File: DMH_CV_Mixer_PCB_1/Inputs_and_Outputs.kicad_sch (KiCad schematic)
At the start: 13 parts, among them J1 TS_Jack_6.35mm_Sw, J10 TS_Jack_6.35mm_Sw, J11 TS_Jack_6.35mm_Sw, J12 TS_Jack_6.35mm_Sw, J2 TS_Jack_6.35mm_Sw, J3 TS_Jack_6.35mm_Sw, J4 TS_Jack_6.35mm_Sw, J5 TS_Jack_6.35mm_Sw, J50 Conn_01x16, J6 TS_Jack_6.35mm_Sw, J7 TS_Jack_6.35mm_Sw, J8 TS_Jack_6.35mm_Sw, J9 TS_Jack_6.35mm_Sw

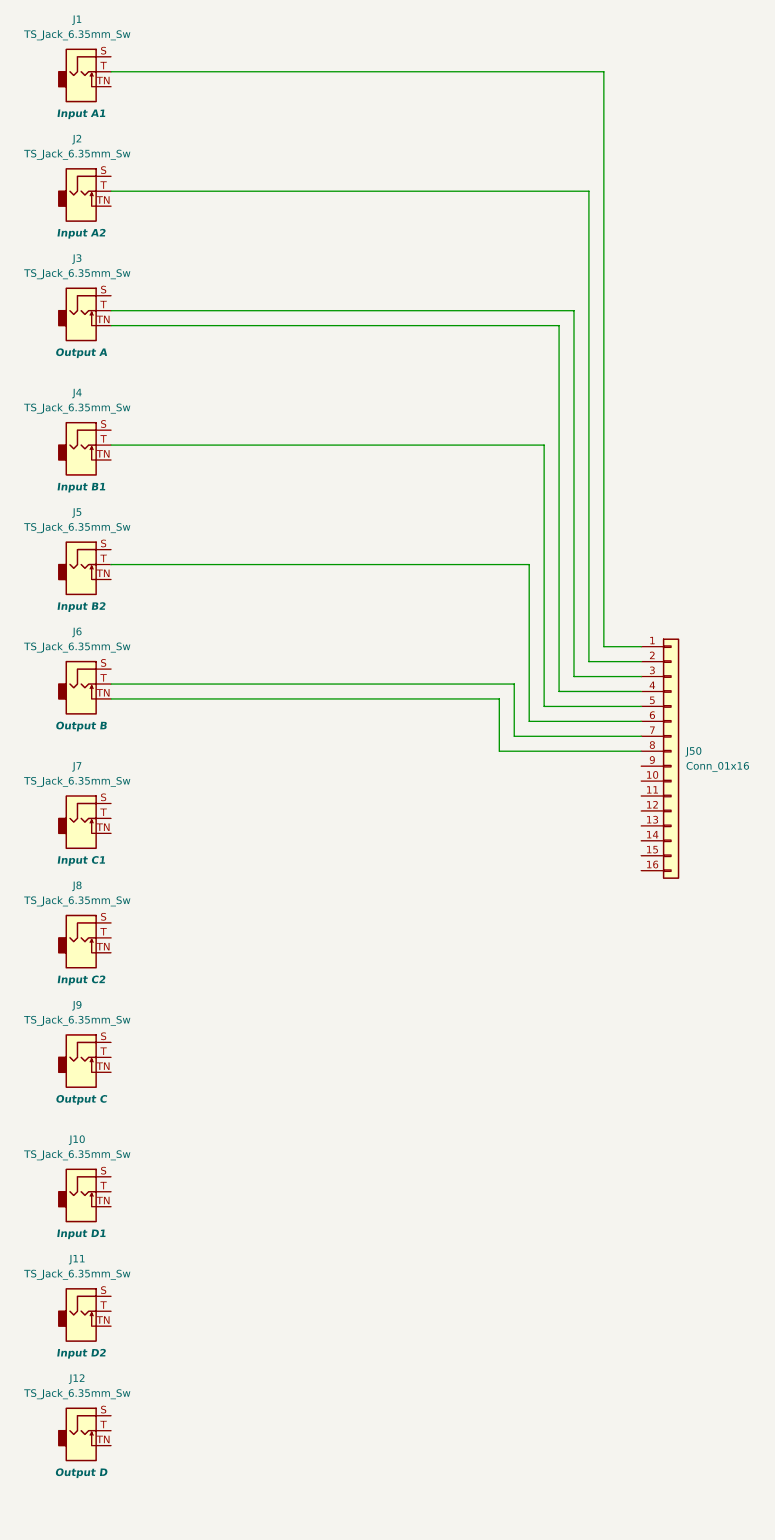
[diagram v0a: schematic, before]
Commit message: Finished IO page
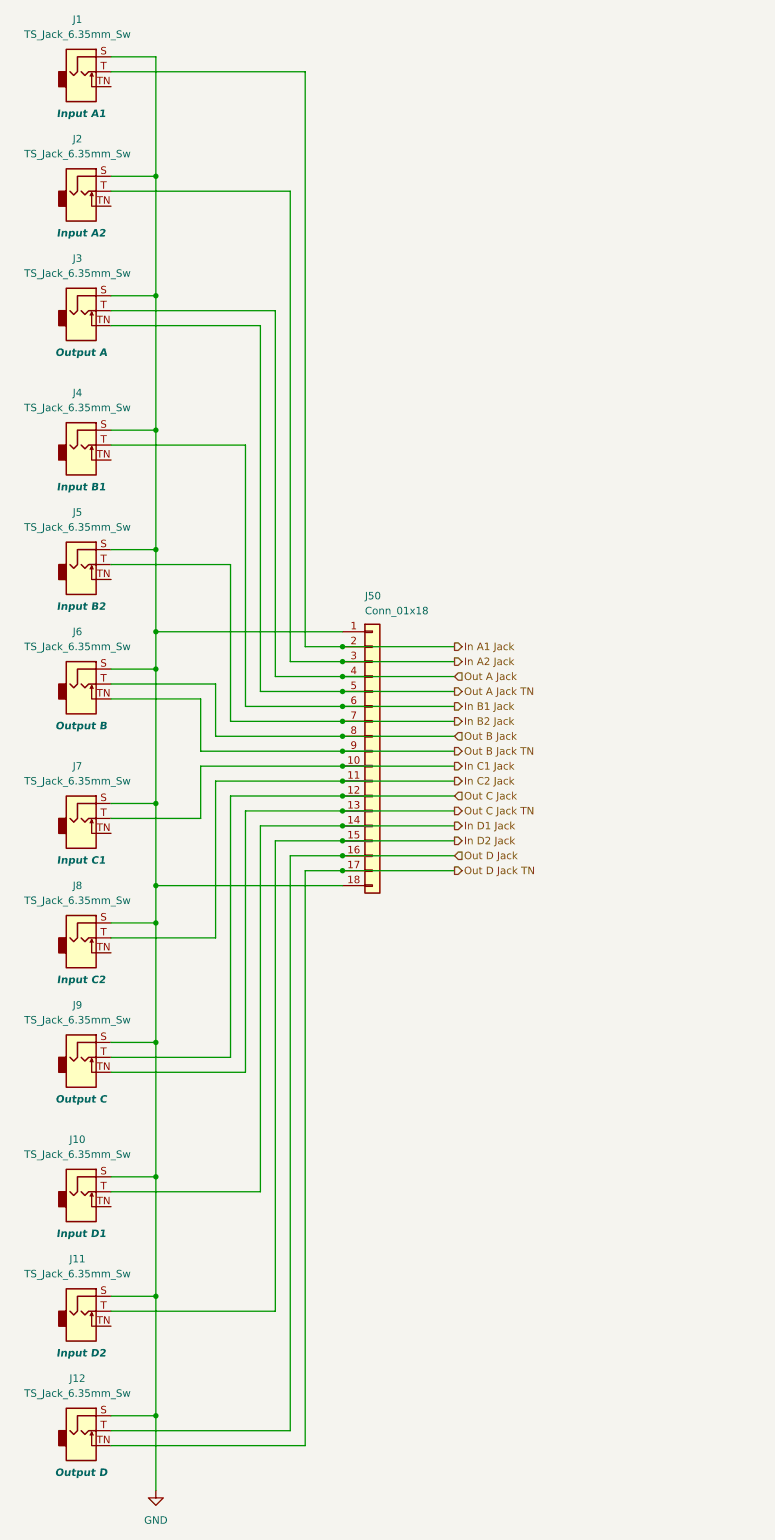
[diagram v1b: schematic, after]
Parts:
- J50: value Conn_01x16 -> Conn_01x18; footprint Connector_PinHeader_2.54mm:PinHeader_1x16_P2.54mm_Vertical -> Connector_PinHeader_2.54mm:PinHeader_1x18_P2.54mm_Vertical; symbol Connector_Generic:Conn_01x16 -> Connector_Generic:Conn_01x18
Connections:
- net GND: now reaches J7.S
- net GND: now also J1.S, J10.S, J11.S, J12.S, J2.S, J3.S, J4.S, J5.S, J50.1 (Pin_1), J50.18 (Pin_18), J6.S, J8.S, J9.S
- net In C1 Jack: now reaches J7.T
- net In C1 Jack: now also J50.10 (Pin_10)
- net In D2 Jack: now reaches J11.T
- net In D2 Jack: now also J50.15 (Pin_15)
- net In A1 Jack: now reaches J1.T
- net In A1 Jack: now also J50.2 (Pin_2); no longer J50.1 (Pin_1)
- net In C2 Jack: now reaches J50.11 (Pin_11)
- net In C2 Jack: now also J8.T
- net Out C Jack: now reaches J50.12 (Pin_12)
- net Out C Jack: now also J9.T
- net Out C Jack TN: now reaches J50.13 (Pin_13)
- net Out C Jack TN: now also J9.TN
- net In D1 Jack: now reaches J50.14 (Pin_14)
- net In D1 Jack: now also J10.T
- net Out D Jack: now reaches J50.16 (Pin_16)
- net Out D Jack: now also J12.T
- net In A2 Jack: now reaches J2.T
- net In A2 Jack: now also J50.3 (Pin_3); no longer J50.2 (Pin_2)
- net Out A Jack: now reaches J3.T
- net Out A Jack: now also J50.4 (Pin_4); no longer J50.3 (Pin_3)
- net Out A Jack TN: now reaches J3.TN
- net Out A Jack TN: now also J50.5 (Pin_5); no longer J50.4 (Pin_4)
- net In B1 Jack: now reaches J4.T
- net In B1 Jack: now also J50.6 (Pin_6); no longer J50.5 (Pin_5)
- net In B2 Jack: now reaches J5.T
- net In B2 Jack: now also J50.7 (Pin_7); no longer J50.6 (Pin_6)
- net Out B Jack: now reaches J6.T
- net Out B Jack: now also J50.8 (Pin_8); no longer J50.7 (Pin_7)
- net Out B Jack TN: now reaches J6.TN
- net Out B Jack TN: now also J50.9 (Pin_9); no longer J50.8 (Pin_8)
- net Out D Jack TN: now reaches J12.TN
- net Out D Jack TN: now also J50.17 (Pin_17)
